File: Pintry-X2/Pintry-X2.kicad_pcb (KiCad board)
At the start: 4 copper layers, 100 x 100 mm, 193 parts, among them J1 USB_B_Micro, J10 1735284-3, J11 54-00131, J2 USB_A, J3 JD0-0001NL, J4 DM3D-SF, J5 UART, J6 Expansion, J7 Fan, J8 Fan, J9 1735284-3, Q1 BSS138PW, Q2 BSS138PW, Q3 BSS138PW, Q5 SIA483DJ, Q6 BC857BW, Q7 SIA483DJ, SW1 SW_Push, U1 TPD4EUSB30, U10 SST25VF512A, U11 TPD4EUSB30, U12 TPD4EUSB30, U13 AP62600, U14 FSUSB30MUX, U15 MIC2005-0.5LYM5, U2 TPD4EUSB30, U3 SN74LVC1G17, U4 74AHCT1G126, U5 TPD4EUSB30, U6 TPD4EUSB30, U7 ASM1061, Y1 ECS-200-12-33-AGN-TR

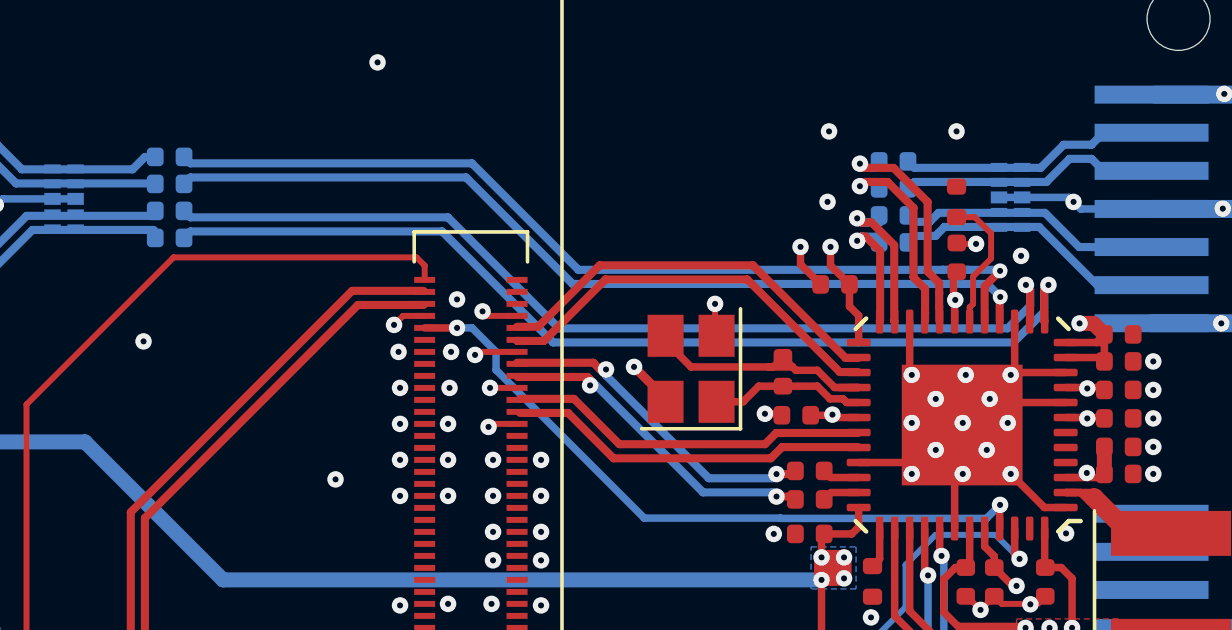
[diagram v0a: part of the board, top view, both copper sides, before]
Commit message: Improved DRC routing. Removed DTO files.
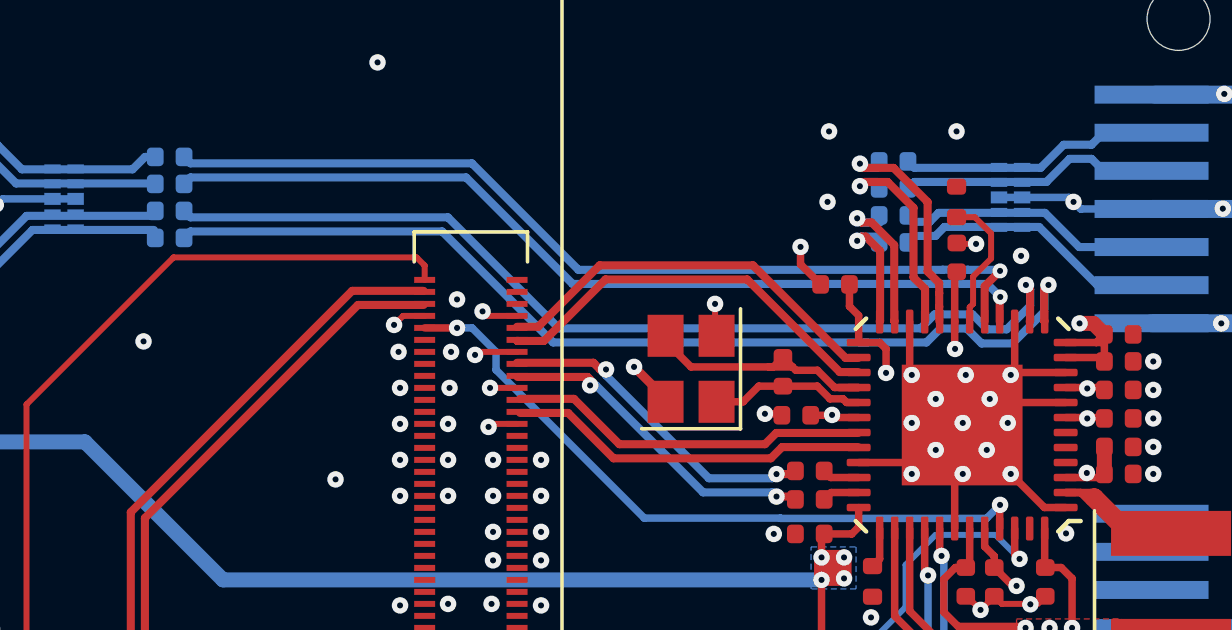
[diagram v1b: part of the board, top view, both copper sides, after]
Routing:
- net +1V2: track 67.2 -> 65.1 mm
- net +3V3: track 362.8 -> 362.3 mm
